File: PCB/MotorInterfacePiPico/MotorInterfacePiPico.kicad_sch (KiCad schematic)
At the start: 1 part, among them U1 RP2040

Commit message: schema nearly finished
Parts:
- removed U1: RP2040, Package_DFN_QFN:QFN-56-1EP_7x7mm_P0.4mm_EP3.2x3.2mm, symbol MCU_RaspberryPi:RP2040
- added C3, C5: 1uF, symbol F2018-cache:C
- added D1, D2: LED, symbol 00TJR:LED
- added J1: Main Power +12V, symbol Connector:Screw_Terminal_01x02
- added J2: Motor Connector, symbol Connector:Conn_01x06_Pin
- added J4: Screw_Terminal_01x06, symbol Connector:Screw_Terminal_01x06
- added Q1, Q2, Q3, Q4: BS170, Package_TO_SOT_THT:TO-92_Inline, symbol 00TJR:BS170_copy
- added R10, R11, R12, R13, R5, R6, R7, R8: 10k, symbol S2020-cache:Device_R_US
- added R14: 5.1k, symbol S2020-cache:Device_R_US
- added R3, R4: R, symbol 00TJR:R
- added R9: 47k, symbol S2020-cache:Device_R_US
- added U1: LM79L05_TO92, Package_TO_SOT_THT:TO-92_Inline, symbol Regulator_Linear:LM79L05_TO92
- added U2: Pico, RPi_Pico:RPi_Pico_SMD_TH, symbol MCU_RaspberryPi_and_Boards:Pico
- added U3: LM7810_TO220, Package_TO_SOT_THT:TO-220-3_Vertical, symbol Regulator_Linear:LM7810_TO220
- added U5: LTV-847, Package_DIP:DIP-16_W7.62mm, symbol Isolator:LTV-847
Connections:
- new net: Q2.1 (D), R8.2, R9.1
- new net: Q1.1 (D), Q2.2 (G), R5.1, R7.2
- new net: Q3.1 (D), Q4.2 (G), R11.2, R12.1
- new net: Q4.1 (D), R13.2, R14.1
- new net: Q1.2 (G), R6.1, U2.25 (GPIO19)
- new net: D1.2 (A), U2.21 (GPIO16)
- new net: D2.2 (A), U2.22 (GPIO17)
- new net: Q3.2 (G), R10.1, U2.24 (GPIO18)
- new net: D2.1 (K), R4.1
- new net: D1.1 (K), R3.1
- new net +10V: R11.1, R13.1, R7.1, R8.1, U1.2 (VI), U3.3 (VO)
- new net +12V: J1.2 (Pin_2), J2.1 (Pin_1), J4.6 (Pin_6), U3.1 (VI)
- new net +5V: J2.4 (Pin_4), U1.3 (VO)
- new net A: J2.5 (Pin_5), U2.4 (GPIO2)
- new net Analog Position: J4.3 (Pin_3)
- new net Analog Speed: J4.5 (Pin_5)
- new net Analog Speed x10: J4.4 (Pin_4)
- new net B: J2.6 (Pin_6), U2.5 (GPIO3)
- new net GND: C3.2, C5.2, J1.1 (Pin_1), J2.2 (Pin_2), J2.3 (Pin_3), J4.1 (Pin_1), Q1.3 (S), Q2.3 (S), Q3.3 (S), Q4.3 (S), R10.2, R12.2, R3.2, R4.2, R5.2, R6.2, U1.1 (GND), U2.12 (GPIO9), U2.18 (GND), U2.23 (GND), U2.28 (GND), U2.3 (GND), U2.38 (GND), U2.8 (GND), U3.2 (GND)
- new net Limit Switch: J4.2 (Pin_2)
- new net Speed Analog: C3.1, C5.1, R14.2, R9.2
- new net V+: U2.39 (VSYS)
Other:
- note added: "PWM to Analog Voltage"

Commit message: clean up PICO schema
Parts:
- removed C3, C5: 1uF, symbol F2018-cache:C
- removed J1: Main Power +12V, symbol Connector:Screw_Terminal_01x02
- removed Q1, Q2, Q3, Q4: BS170, Package_TO_SOT_THT:TO-92_Inline, symbol 00TJR:BS170_copy
- removed R10, R11, R12, R13, R5, R6, R7, R8: 10k, symbol S2020-cache:Device_R_US
- removed R14: 5.1k, symbol S2020-cache:Device_R_US
- removed R9: 47k, symbol S2020-cache:Device_R_US
- removed U1: LM79L05_TO92, Package_TO_SOT_THT:TO-92_Inline, symbol Regulator_Linear:LM79L05_TO92
- removed U3: LM7810_TO220, Package_TO_SOT_THT:TO-220-3_Vertical, symbol Regulator_Linear:LM7810_TO220
- removed U5: LTV-847, Package_DIP:DIP-16_W7.62mm, symbol Isolator:LTV-847
- added C1, C2, C3: 1uF, symbol Device:C
- added Q1, Q2, Q3: 2N3904, TO-92, symbol 00TJR:2N3904
- added R1, R10, R11, R12, R13, R17, R2, R3, R4, R7, R8, R9: 10k, symbol 00TJR:R
- added R14, R16: 5.1k, symbol 00TJR:R
- added R15: 47k, symbol 00TJR:R
- added U2: OPA4197, Package_SO:TSSOP-14_4.4x5mm_P0.65mm, symbol Amplifier_Operational:OPA4197xPW
- R5: renamed from R3; value R -> 330
- R6: renamed from R4; value R -> 330
- renumbered J2 to J1, J4 to J2, U2 to U1
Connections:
- net Analog Speed x10 is gone; now on net Analog Position: J2.4 (Pin_4)
- net V+ is gone; now on net +5V: U1.39 (VSYS)
- net A: now also Q1.~ (E); no longer U1.4 (GPIO2)
- net Analog Position: now also C3.1, R16.2; no longer J2.3 (Pin_3)
- net Analog Speed: now also C2.1, R15.2
- net B: now also Q2.~ (E); no longer U1.5 (GPIO3)
- net GND: now also C1.2, C2.2, C3.2, R10.2, R11.2, R12.2; no longer U1.28 (GND), U1.3 (GND)
- net Limit Switch: now also U1.27 (GPIO21), Q3.~ (E), R17.2; no longer J2.2 (Pin_2)
- net PWM Speed: now reaches U1.25 (GPIO19)
- net PWM Speed: now also U2.5 (+)
- net PWM Position: now reaches U1.24 (GPIO18)
- net PWM Position: now also U2.10 (+)
- net PWM Position x10: now reaches U1.26 (GPIO20)
- net PWM Position x10: now also U2.3 (+)
- net +3.3V: now reaches U1.36 (3V3)
- net +3.3V: now also R1.1, R13.1, R17.1, R2.1, R3.1, R4.1, R7.1, R8.1, R9.1
- new net: J2.2 (Pin_2), Q3.~ (E)
- new net: R11.1, R8.2, U2.6 (-)
- new net: R10.1, R7.2, U2.2 (-)
- new net: Q1.~ (E), R3.2, U1.4 (GPIO2)
- new net: Q2.~ (E), R4.2, U1.5 (GPIO3)
- new net: Q1.~ (E), R1.2
- new net: R12.1, R9.2, U2.9 (-)
- new net: R15.1, U2.7
- new net: Q3.~ (E), R13.2
- new net: R16.1, U2.8
- new net: R14.1, U2.1
- new net: Q2.~ (E), R2.2
- new net Analog Position x10: C1.1, J2.3 (Pin_3), R14.2
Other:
- added sheet Power (untitled.kicad_sch)
- note added: "Main Interface Terminals Power / PLC / Limit Switch"
- note added: "Motor / Encoder Connector"
- note added: "PWM Level Transition and Integration to Analog DC Voltage 0 - 10V"
- note added: "Raspberry Pi PICO Note: Place decouple near VSYS"
- note removed: "PWM to Analog Voltage"
- company: (none) -> ISU
- title: (none) -> PICO Motor Interface
- moved on the sheet: D1, D2, J1, J2, R5, R6, U1

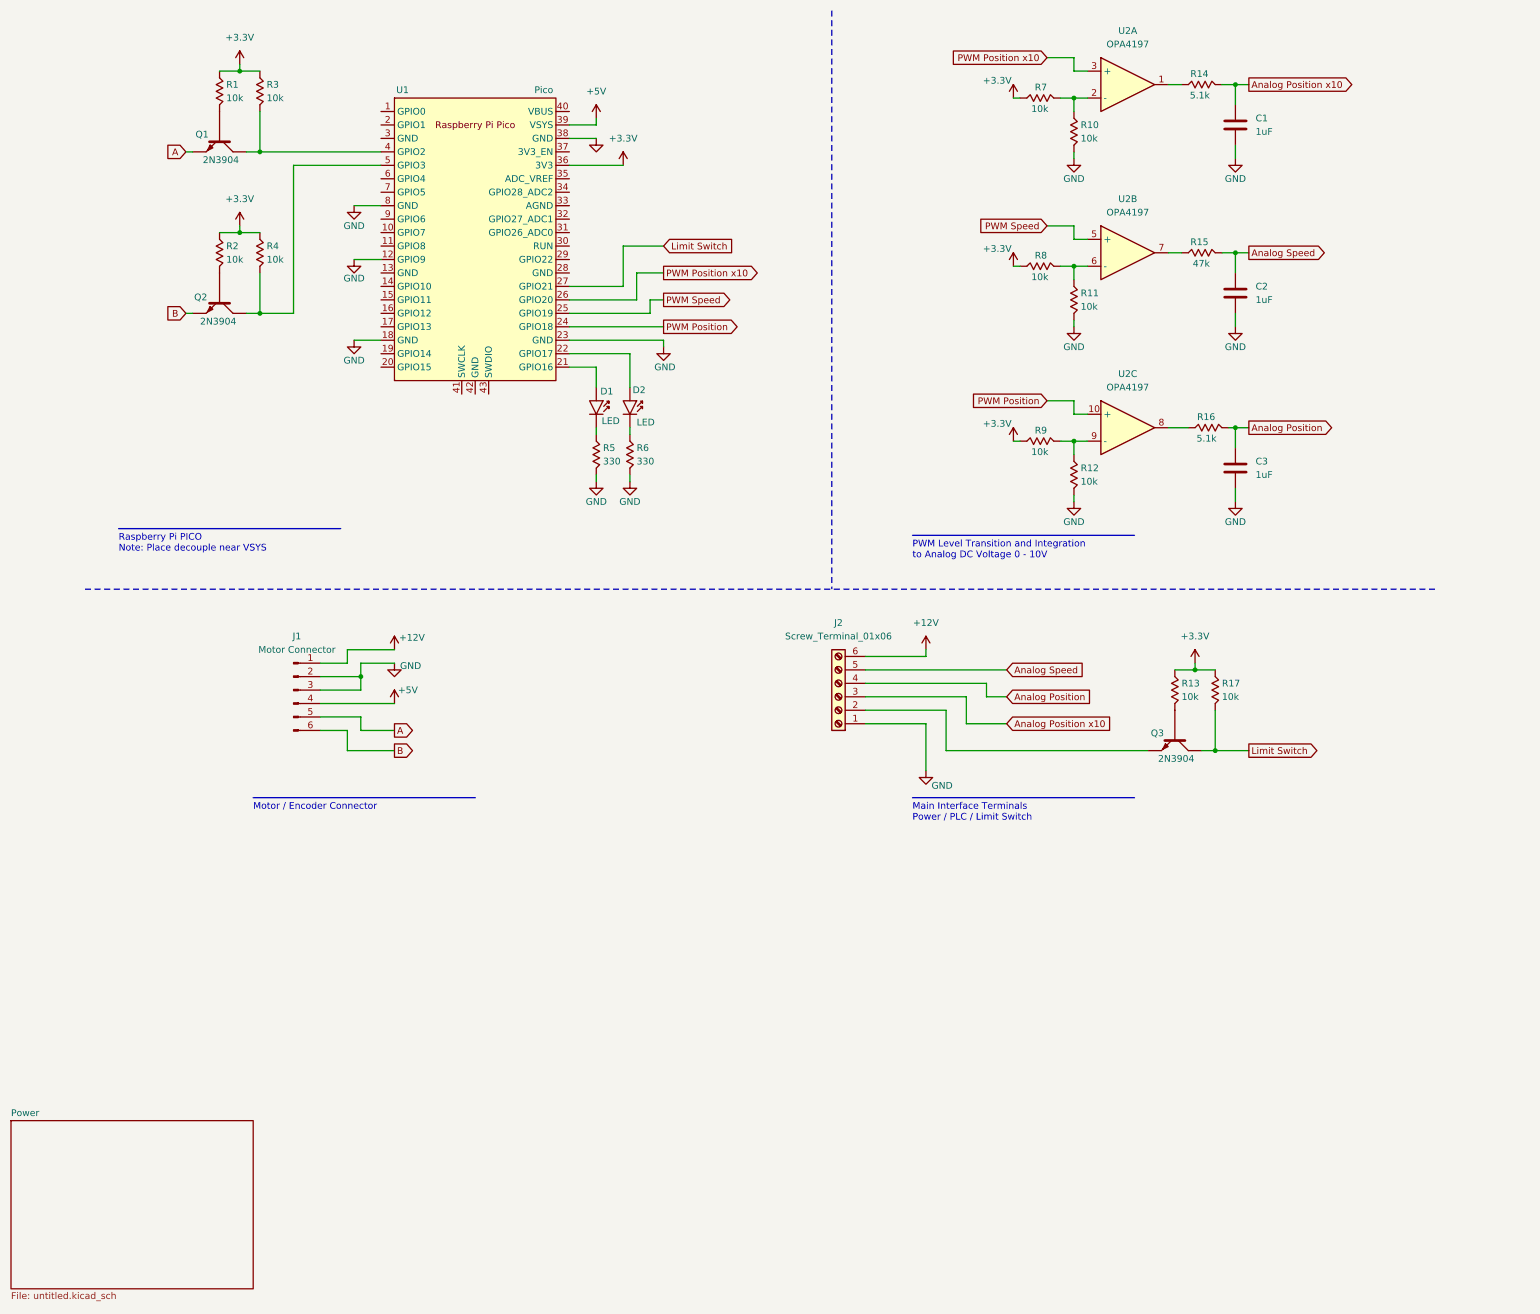
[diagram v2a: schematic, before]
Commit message: Layout complete, need silkscreen and BOM
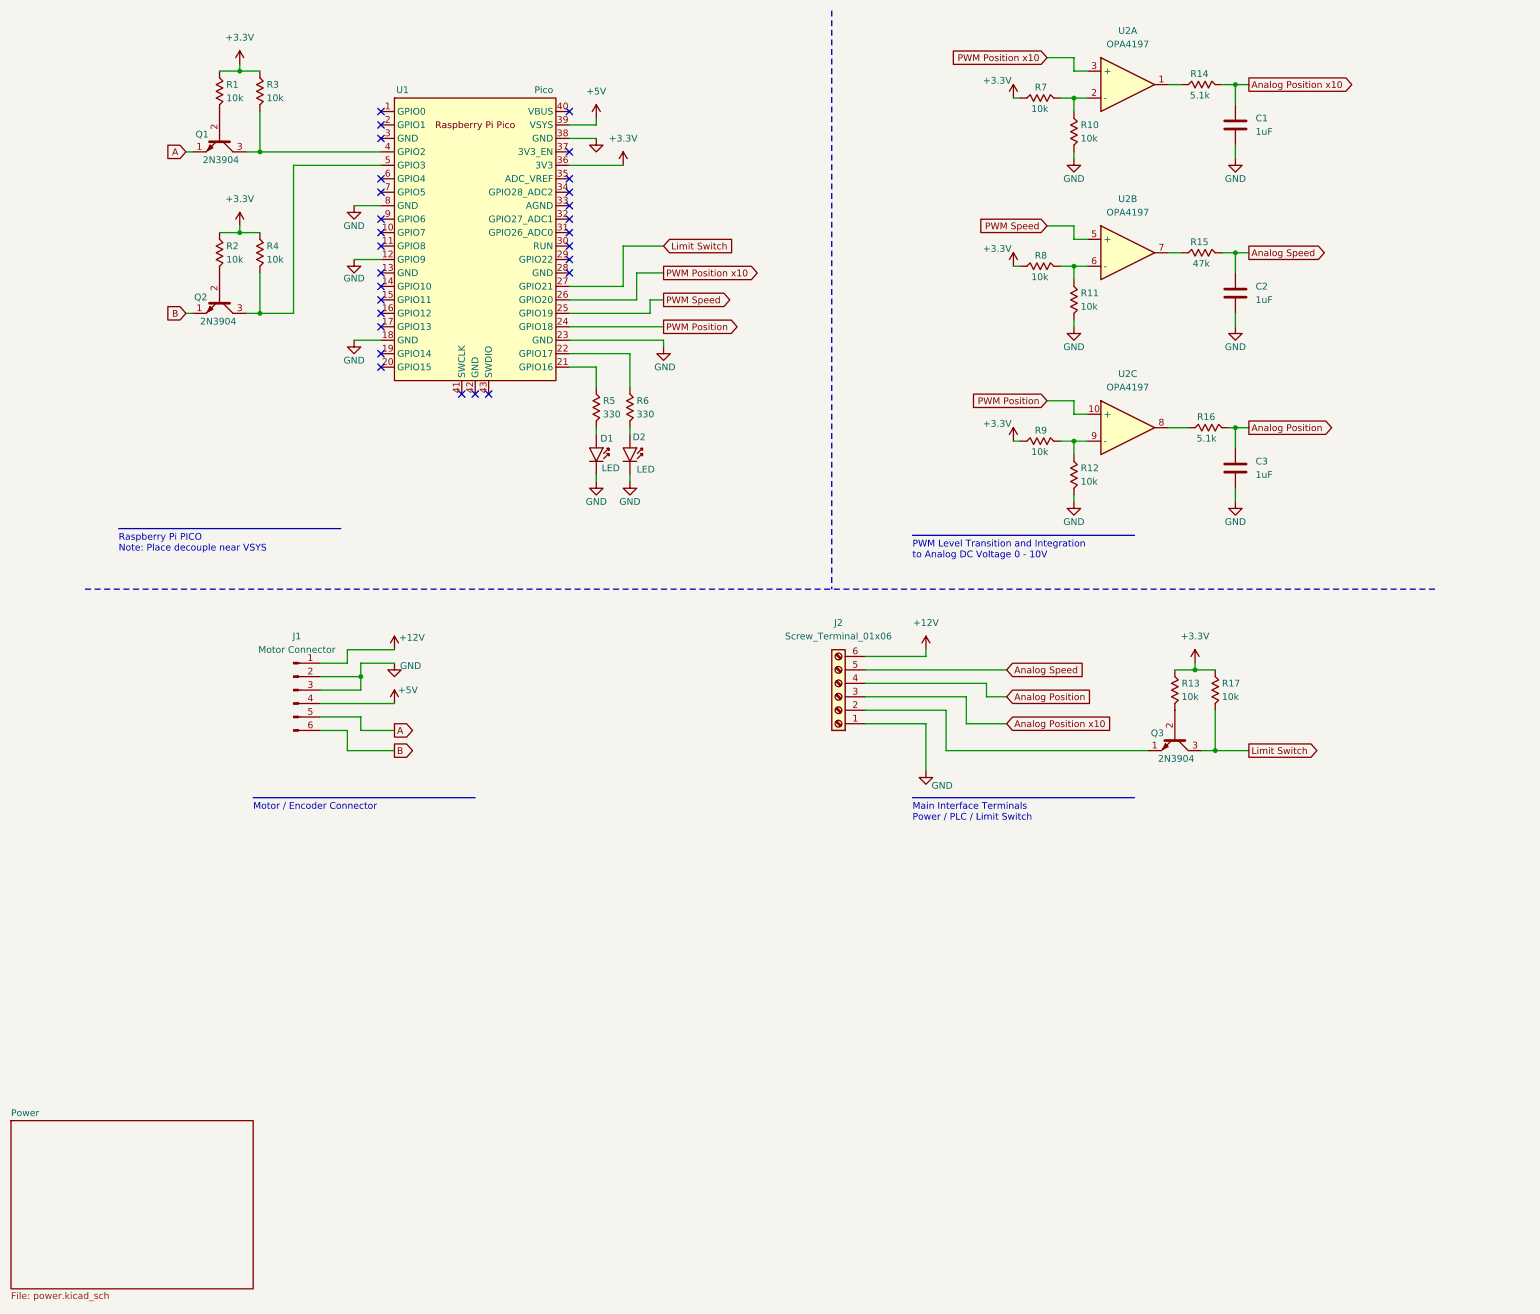
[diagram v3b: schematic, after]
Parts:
- C1, C2: footprint (none) -> TJR:C_Rect_L7.3mm_W4.5_H9.5mm_P5.0mmx
- C3: footprint (none) -> TJR:C_Rect_L7.3mm_W4.5_H9.5mm_P5.0mmx; digikey (none) -> https://www.digikey.com/en/products/detail/epcos-tdk-electr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
- D1, D2: footprint (none) -> TSL:LED_D3.0mm
- J1: footprint (none) -> Connector_JST:JST_XH_B6B-XH-A_1x06_P2.50mm_Vertical
- J2: footprint (none) -> TerminalBlock_Phoenix:TerminalBlock_Phoenix_PT-1,5-6-5.0-H_1x06_P5.00mm_Horizontal
- Q1, Q2, Q3: footprint TO-92 -> TJR:TO-92-3_Formed_Leads; symbol 00TJR:2N3904 -> TJR:2N3904
- R1, R10, R11, R12, R13, R14, R15, R16, R17, R2, R3, R4, R5, R6, R7, R8, R9: footprint (none) -> TJR:R_Axial_DIN0207_L6.3mm_D2.5mm_P7.62mm_Horizontal; symbol 00TJR:R -> TJR:R; digikey (none) -> https://www.digikey.com/en/products/detail/stackpole-electr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
- U1: footprint RPi_Pico:RPi_Pico_SMD_TH -> TJR:RPi_Pico_SMD_TH
- U2: footprint Package_SO:TSSOP-14_4.4x5mm_P0.65mm -> Package_SO:SOIC-14_3.9x8.7mm_P1.27mm
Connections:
- net A: now also Q1.1 (E); no longer Q1.~ (E)
- net B: now also Q2.1 (E); no longer Q2.~ (E)
- net GND: now also D1.1 (K), D2.1 (K); no longer R5.2, R6.2
- net Limit Switch: now also Q3.3 (C); no longer Q3.~ (E)
- net at J2.2 (Pin_2): now also Q3.1 (E); no longer Q3.~ (E)
- net at U1.21 (GPIO16): now also R5.1; no longer D1.2 (A)
- net at U1.22 (GPIO17): now also R6.1; no longer D2.2 (A)
- net at R3.2, U1.4 (GPIO2): now also Q1.3 (C); no longer Q1.~ (E)
- net at R4.2, U1.5 (GPIO3): now also Q2.3 (C); no longer Q2.~ (E)
- net at R1.2: now also Q1.2 (B); no longer Q1.~ (E)
- net at R13.2: now also Q3.2 (B); no longer Q3.~ (E)
- net at R2.2: now also Q2.2 (B); no longer Q2.~ (E)
- new net: D2.2 (A), R6.2
- new net: D1.2 (A), R5.2
- no-connect marks 0 -> 28
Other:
- sheet Power: file untitled.kicad_sch -> power.kicad_sch
- moved on the sheet: D1, D2, R5, R6

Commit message: Layout complete, need BOM
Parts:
- U2: footprint Package_SO:SOIC-14_3.9x8.7mm_P1.27mm -> TJR:D14_TEX
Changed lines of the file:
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@@
 			)
 		)
-		(property "Footprint" "Package_SO:SOIC-14_3.9x8.7mm_P1.27mm"
+		(property "Footprint" "TJR:D14_TEX"
 			(at 209.55 91.44 0)
 			(effects
@@
 			)
 		)
-		(property "Footprint" "Package_SO:SOIC-14_3.9x8.7mm_P1.27mm"
+		(property "Footprint" "TJR:D14_TEX"
 			(at 209.55 26.67 0)
 			(effects
@@
 			)
 		)
-		(property "Footprint" "Package_SO:SOIC-14_3.9x8.7mm_P1.27mm"
+		(property "Footprint" "TJR:D14_TEX"
 			(at 209.55 58.42 0)
 			(effects

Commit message: add MotorInterfacePiPico
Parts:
- C1, C2: digikey (none) -> https://www.digikey.com/en/products/detail/epcos-tdk-electr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
- U1: digikey (none) -> https://www.digikey.com/en/products/detail/texas-instrument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
- U2: Notes (none) -> 14-SOIC (0.154", 3.90mm Width); digikey (none) -> https://www.digikey.com/en/products/detail/texas-instrument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
